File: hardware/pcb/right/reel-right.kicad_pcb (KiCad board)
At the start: 2 copper layers, 134.6 x 86.9 mm, 46 parts, among them J1 Conn_01x02, SW1 SW_Push, SW10 SW_Push, SW11 SW_Push, SW12 SW_Push, SW13 SW_Push, SW14 SW_Push, SW15 SW_Push, SW16 SW_Push, SW17 SW_Push, SW18 SW_Push, SW19 SW_Push, SW2 SW_Push, SW22 SW_SPDT, SW3 SW_Push, SW4 SW_Push, SW5 SW_Push, SW6 SW_Push, SW7 SW_Push, SW8 SW_Push, SW9 SW_Push

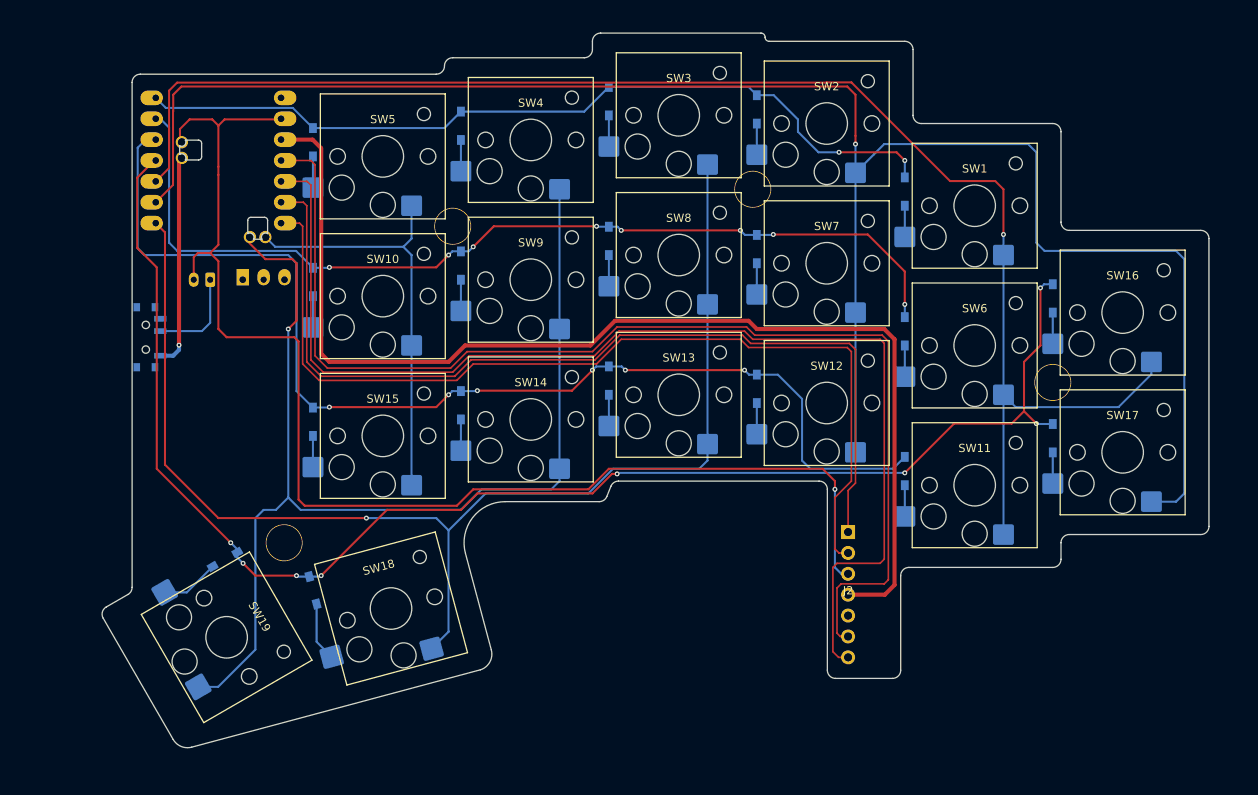
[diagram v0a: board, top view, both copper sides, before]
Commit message: Reorganize hardware and add ZMK firmware
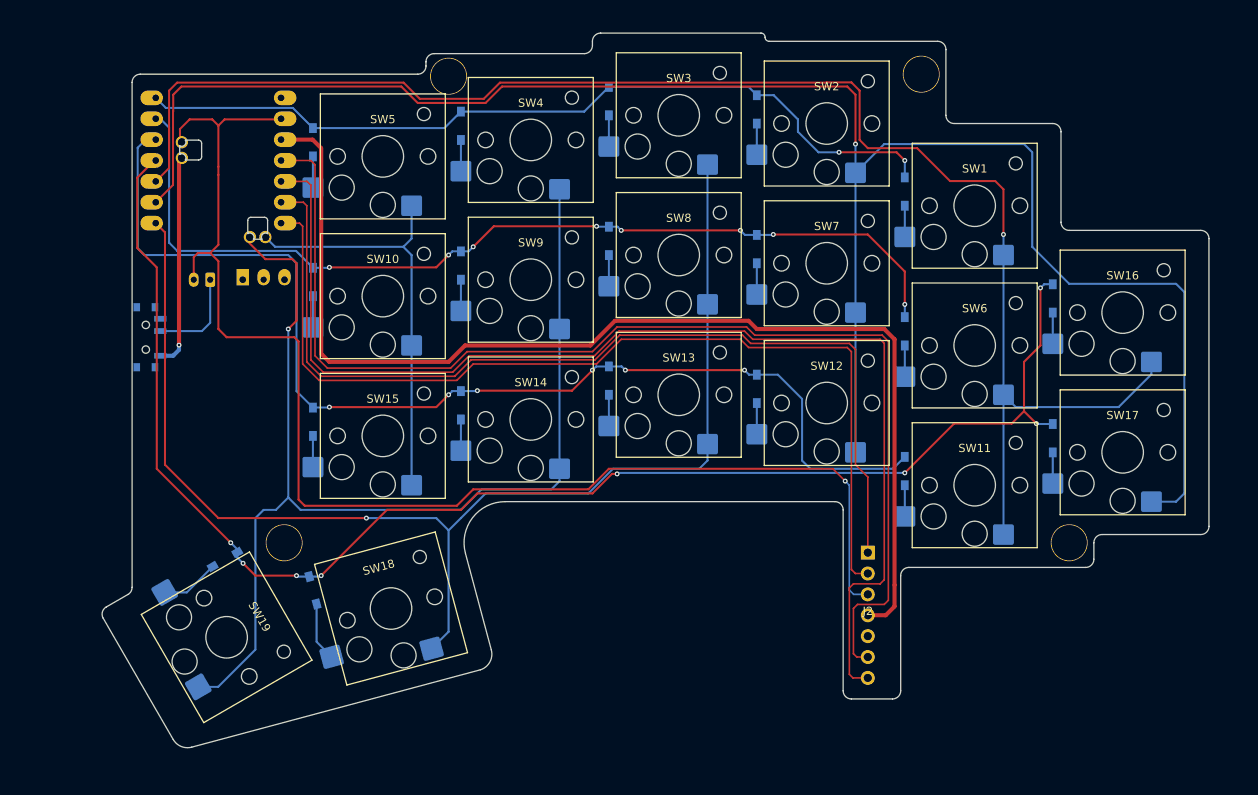
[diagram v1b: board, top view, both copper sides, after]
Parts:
- moved Ref** 24.8 mm to (145.5, 50.5)
- moved Ref** 19.6 mm to (163.5, 107.5)
- moved Ref** 18.3 mm to (88.0, 50.8)
- moved J2 3.47 mm to (139.0, 116.3)
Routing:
- net Col0: track 182.8 -> 187.9 mm
- net GND: track 155.4 -> 160.2 mm
- net SCLK: track 115.1 -> 117.5 mm
- net nCS: track 116.4 -> 118.5 mm
- net MOTION: track 143.4 -> 144.5 mm
- net SDIO: track 143.4 -> 144.3 mm
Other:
- outline, holes or cut-outs redrawn

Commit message: Update PCB layouts and mechanical assets
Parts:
- added J3: Conn_01x05, reel:Display_BeeKeeb_MIP_1.08in_LS011B7DH03, F.Cu at (60.2, 101.2)
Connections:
- U1 pad 17: unconnected-(U1-NFC3_0.16-Pad17) -> SI
- U1 pad 18: unconnected-(U1-NFC4_1.00-Pad18) -> SCK
- U1 pad 19: unconnected-(U1-NFC5_1.10-Pad19) -> CS
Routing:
- net 3.3V: track 139.7 -> 189.3 mm, vias 0 -> 2
- net CS: track 0.00 -> 27.3 mm
- net SCK: track 0.00 -> 27.0 mm
- net SI: track 0.00 -> 26.8 mm
- net GND: track 160.2 -> 186.2 mm
- net Row3: track 181.1 -> 185.8 mm
- net Col2: track 153.9 -> 157.1 mm

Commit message: Update ReeL hardware and fabrication assets
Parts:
- added Ref**: Val**, reel:m2_Spacer_Hole, F.Cu at (137.5, 107.5)
- J1: footprint Connector_JST:JST_PH_S2B-PH-K_1x02_P2.00mm_Horizontal -> reel:JST_S2B-PH-SM4-TB
- moved J3 12.2 mm to (60.2, 89.0)
- moved D18 10.0 mm to (60.8, 110.6)
- moved D19 10.0 mm to (53.2, 108.1)
- moved J2 10.0 mm to (129.0, 116.3)
- moved Ref** 10.0 mm to (58.0, 107.5)
- moved SW18 10.0 mm to (71.0, 115.5)
- moved SW19 10.0 mm to (51.0, 119.0)
- moved J1 5.65 mm to (58.5, 69.9)
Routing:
- net GND: track 186.2 -> 156.5 mm, vias 1 -> 2
- net 3.3V: track 189.3 -> 166.6 mm
- net SDIO: track 144.3 -> 130.4 mm, vias 0 -> 1
- net MOTION: track 144.5 -> 131.2 mm, vias 0 -> 1
- net CS: track 27.3 -> 14.6 mm
- net SCK: track 27.0 -> 14.6 mm
- net SI: track 26.8 -> 14.6 mm
- net Col3: track 136.1 -> 147.6 mm
- net nCS: track 118.5 -> 107.3 mm
- net SCLK: track 117.5 -> 110.5 mm
- net Row3: track 185.8 -> 192.2 mm, vias 8 -> 5
- net Net-(J1-Pin_1): track 11.7 -> 17.3 mm, vias 0 -> 2
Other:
- board size 134.6 x 86.9 mm -> 143 x 86.6 mm

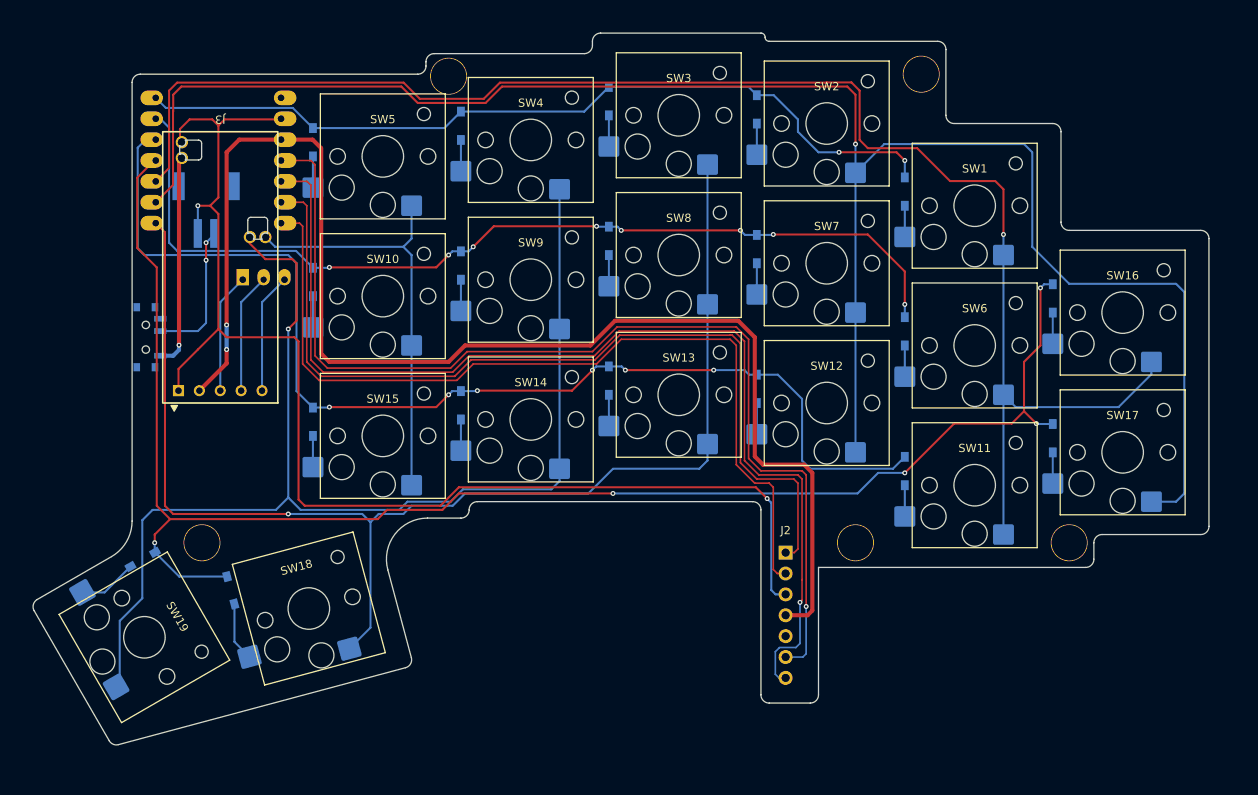
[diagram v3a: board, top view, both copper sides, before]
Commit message: Update right plate PCB models
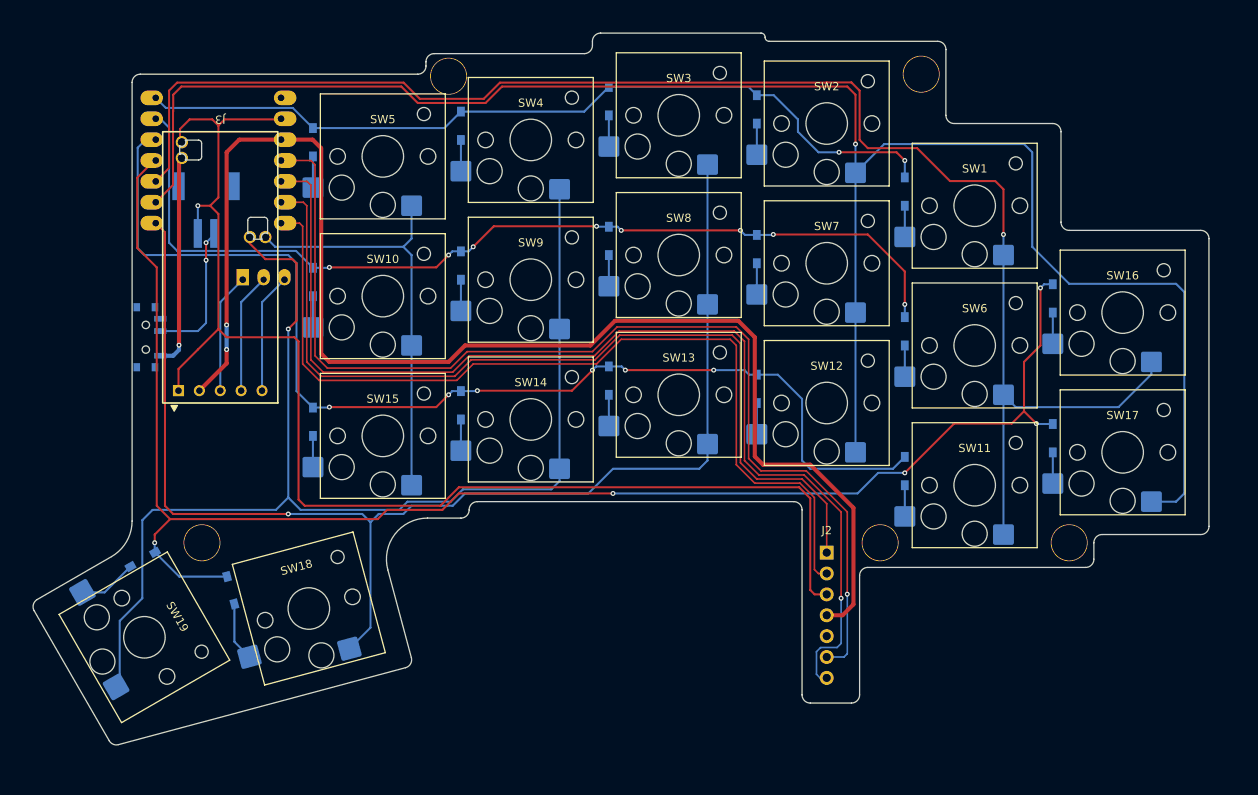
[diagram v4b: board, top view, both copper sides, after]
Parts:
- moved J2 5.00 mm to (134.0, 116.3)
- moved Ref** 3.00 mm to (140.5, 107.5)
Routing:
- net GND: track 156.5 -> 161.8 mm, vias 2 -> 1
- net nCS: track 107.3 -> 111.6 mm
- net SDIO: track 130.4 -> 132.8 mm
- net MOTION: track 131.2 -> 133.5 mm
- net 3.3V: track 166.6 -> 168.6 mm
- net SCLK: track 110.5 -> 111.3 mm
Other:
- outline, holes or cut-outs redrawn

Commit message: Update right PCB and derived variants
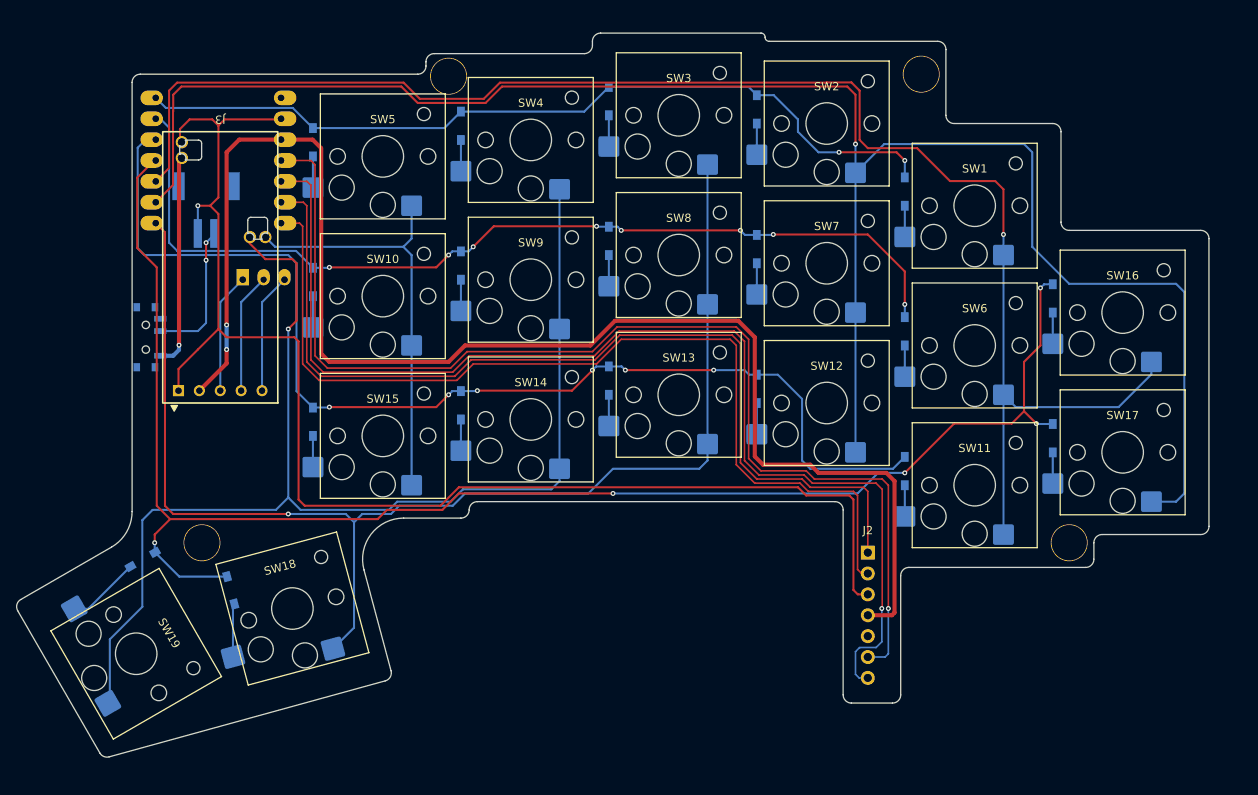
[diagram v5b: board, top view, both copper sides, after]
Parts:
- removed the Ref** at (140.5, 107.5)
- moved J2 5.00 mm to (139.0, 116.3)
- moved SW19 2.24 mm to (50.0, 121.0)
- moved SW18 2.00 mm to (69.0, 115.5)
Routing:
- net 3.3V: track 168.6 -> 176.1 mm
- net MOTION: track 133.5 -> 140.4 mm
- net SDIO: track 132.8 -> 139.7 mm
- net SCLK: track 111.3 -> 117.2 mm
- net nCS: track 111.6 -> 116.8 mm
- net GND: track 161.8 -> 166.7 mm
- net Net-(D19-A): track 7.15 -> 8.98 mm
- net Col3: track 147.6 -> 149.2 mm
- net Net-(D18-A): track 7.18 -> 6.49 mm
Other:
- board size 143 x 86.6 mm -> 145 x 88.1 mm

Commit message: Publish current hardware and fabrication assets
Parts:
- J1: footprint reel:JST_S2B-PH-SM4-TB -> Connector_JST:JST_PH_S2B-PH-K_1x02_P2.00mm_Horizontal
- moved Ref** 19.6 mm to (165.0, 88.0)
- moved Ref** 17.2 mm to (88.0, 68.0)
- moved J3 14.5 mm to (59.0, 103.5)
- moved Ref** 13.5 mm to (145.0, 64.0)
- moved D1 6.87 mm to (146.5, 55.8)
- moved D19 5.83 mm to (50.2, 113.1)
- moved D18 4.43 mm to (59.5, 114.8)
- moved D16 4.12 mm to (165.5, 74.0)
- moved D17 4.12 mm to (165.5, 93.0)
- moved SW16 4.12 mm to (174.0, 78.5)
- moved SW17 4.12 mm to (174.0, 97.5)
- moved D11 3.61 mm to (146.5, 98.0)
- moved SW1 3.61 mm to (155.0, 64.5)
- moved SW11 3.61 mm to (155.0, 102.5)
- moved D6 3.00 mm to (146.5, 79.0)
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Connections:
- J3 pad 1: GND -> SI
- J3 pad 2: 3.3V -> SCK
- J3 pad 3: SI -> 3.3V
- J3 pad 4: SCK -> GND
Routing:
- net Col1: track 227.5 -> 205.8 mm, vias 1 -> 3
- net Row1: track 116.8 -> 138.3 mm, vias 8 -> 5
- net 3.3V: track 176.1 -> 195.3 mm, vias 2 -> 1
- net GND: track 166.7 -> 185.5 mm, vias 1 -> 5
- net SI: track 14.6 -> 33.3 mm
- net SCK: track 14.6 -> 33.3 mm
- net CS: track 14.6 -> 31.3 mm
- net Col0: track 187.9 -> 204.0 mm, vias 1 -> 2
- net Row3: track 192.2 -> 207.3 mm, vias 5 -> 6
- net Col2: track 157.2 -> 167.7 mm
- net Row2: track 137.5 -> 145.5 mm
- net nCS: track 116.8 -> 122.4 mm, vias 0 -> 1
- net SCLK: track 117.2 -> 122.5 mm
- net Net-(D1-A): track 3.80 -> 9.01 mm
- net MOTION: track 140.4 -> 144.1 mm
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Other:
- board size 145 x 88.1 mm -> 147.7 x 92.6 mm
